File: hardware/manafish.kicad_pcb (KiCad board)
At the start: 4 copper layers, 70 x 90 mm, 118 parts, among them IC1 TPD4EUSB30, IC10 WSEN-PADS_2511020213301, IC11 BMI270, IC12 SHT45-AD1F-R2, IC15 TPS22965DSGR, IC2 TPD4EUSB30, IC3 JXF0-1012NL, IC4 RP2354A, IC5 Ag59824-LPB, IC6 LTV-817S, IC7 LTV-817S, IC8 LTC4162-LAD, IC9 TPSM53604RDA, J1 Conn_01x04_Pin, J11 Conn_01x22_Female, J12 Magnet, J13 Conn_02x06_Odd_Even, J2 SM03B-SRSS-TB, J3 AM32_1, J4 AM32_2, J5 Conn_01x22_Female, J6 Battery, J7 Conn_02x07_Odd_Even, J8 USB_C_Receptacle_USB2.0_14P, J9 Conn_02x08_Odd_Even, Q1 FDMC8327L, Q2 FDMC8327L, Y1 ABM8-272-T3

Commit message: Add switchable ESC power, vertical camera connectors and 3.3 V decoupling
- ESC power switch on the root sheet:
  - Battery input J6 changes to XT60PW-M. New XT60PW-F J14 carries switched
    power to both ESCs.
  - Q3 (onsemi NTMFS5C404NLT1G, 40 V, 0.67 mOhm) is driven by the photovoltaic
    driver IC16 (Vishay VOM1271T) from RP2354A GPIO14 (ESC_PWR_EN) via R31.
  - Soft start C46/D6/R32 keeps Q3 in its SOA while the ESC capacitors charge.
    D7 clamps the gate when the battery is unplugged or the thrusters windmill.
  - Static switch with no current limit: the battery BMS protects. Firmware
    timing rules are in the schematic note and the README.
- Camera connectors J5/J11 are now Molex 501951-2230 (vertical, flip lock).
  The footprint numbers pads n = Molex circuit 23-n so a standard Pi 22-pin
  cable lands GND on pin 1, as on the CM5 IO Board.
- Decoupling: 10 uF + 100 nF at the CM5 3.3 V output, 10 uF at each camera
  supply pin.
- Polyfuses F1-F3 removed; the battery feeds the charger path directly.
- New libraries VOM1271T, NTMFS5C404NL, Molex and Vishay, with 3D models.
- PCB updated from the schematic. The layout will be redone.

Co-Authored-By: Claude Opus 5.5 <noreply@anthropic.com>
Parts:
- removed F1, F2, F3: MF-LSMF260/33X-2, Fuse:Fuse_2920_7451Metric
- added C42: 10uF, Capacitor_SMD:C_0603_1608Metric, F.Cu at (91.6, 108.4)
- added C43: 100n, Capacitor_SMD:C_0402_1005Metric, F.Cu at (91.0, 110.6)
- added C44: 10uF, Capacitor_SMD:C_0603_1608Metric, F.Cu at (91.6, 101.4)
- added C45: 10uF, Capacitor_SMD:C_0603_1608Metric, F.Cu at (91.6, 103.9)
- added C46: 1uF 50V, Capacitor_SMD:C_0603_1608Metric, F.Cu at (81.5, 114.4)
- added D6: 1N4148WS, Diode_SMD:D_SOD-323, F.Cu at (81.7, 108.7)
- added D7: 1N4148WS, Diode_SMD:D_SOD-323, F.Cu at (81.7, 111.6)
- added IC16: VOM1271T, Vishay:Vishay_SOP-4_P2.54mm_VOM1271T, F.Cu at (66.7, 122.4)
- added J14: ESC power, Connector_AMASS:AMASS_XT60PW-F_1x02_P7.20mm_Horizontal, F.Cu at (74.4, 116.5)
- added Q3: NTMFS5C404NL, Package_SO:ONSemi_SO-8FL_488AA, F.Cu at (83.6, 103.7)
- added R31: 180R, Resistor_SMD:R_0402_1005Metric, F.Cu at (81.0, 116.6)
- added R32: 2.2MR, Resistor_SMD:R_0402_1005Metric, F.Cu at (81.0, 118.6)
- J11, J5: footprint CM5IO:Hirose_FH12-22S-0.5SH_1x22-1MP_P0.50mm_Horizontal -> Molex:Molex_501951-2230_1x22-1MP_P0.50mm_Vertical_RPi-CSI
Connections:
- C30 pad 1: /Power Management/BAT+ -> /BAT_IN
- C40 pad 1: /Power Management/BAT+ -> /BAT_IN
- IC4 pad 18: unconnected-(IC4-GPIO14-Pad18) -> /ESC_PWR_EN
- IC8 pad 19: /Power Management/BAT+ -> /BAT_IN
- IC8 pad 20: /Power Management/BAT+ -> /BAT_IN
- J8 pad A4: /VBUS -> unconnected-(J8-VBUS-PadA4)_3
- J8 pad A9: /VBUS -> unconnected-(J8-VBUS-PadA4)_1
- J8 pad B4: /VBUS -> unconnected-(J8-VBUS-PadA4)_2
- J8 pad B9: /VBUS -> unconnected-(J8-VBUS-PadA4)
- R20 pad 2: /Power Management/BAT+ -> /BAT_IN
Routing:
- net /Power Management/BAT+: track 10.4 -> 0.00 mm, vias 6 -> 0
- net /BAT_IN: track 0.00 -> 10.4 mm, vias 0 -> 6
- net /VBUS: track 5.37 -> 0.00 mm
- net (no net): track 0.00 -> 5.37 mm
- added copper zone on F.Cu, net /BAT_IN
- removed copper zone on B.Cu, net /Power Management/BAT+
- removed copper zone on F.Cu, net /Power Management/BAT+

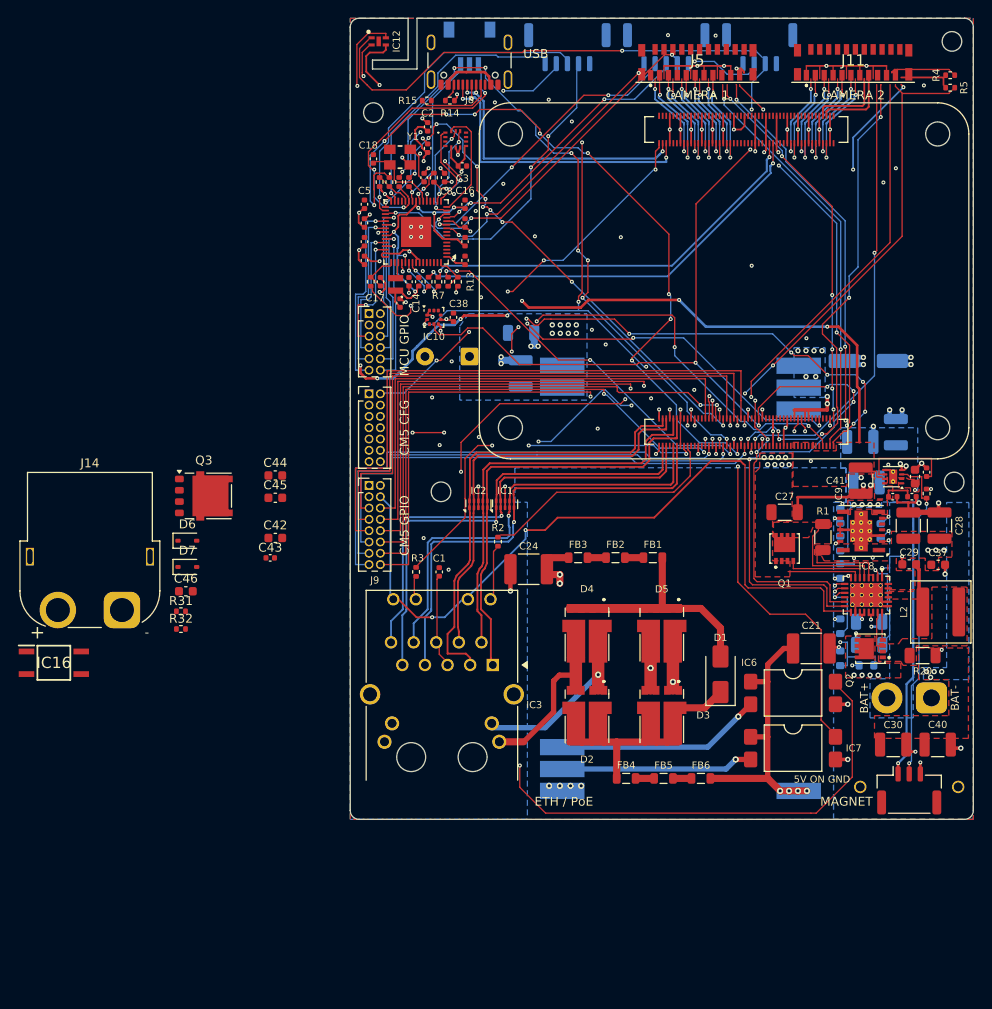
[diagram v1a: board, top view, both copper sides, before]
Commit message: Redo the PCB layout (rev 3): 70 x 109.2 mm, connectors on one side, 45° routing
- All connectors on the top: cameras, USB-C and the magnet switch along the
  top edge, the rest at the bottom around the RJ45, which moves towards the
  centre line; C20 near the centre for the tube radius
- Every part except the PoE module IC5 on the top (reflow one side)
- 45-degree routing only, chamfers at least 1.5 x width, traces bundled to
  keep the planes whole
- Small SHT45 tongue with its bypass cap beside it; planes cut out under L2
  with nothing under it; copper 3.4 mm from the CM5 mounting holes
- Charger and RP2354A regulator laid out per their datasheets
- J3/J4 vertical JST GH (BM05B-GHS-TBT); J8 VBUS label restored
- Edge clearance 0.3 mm, netclass patterns follow the current net names,
  hand-soldered THT GND pins get one thermal spoke
- User.Comments fab/assembly notes and README PCB section updated for rev 3

Co-Authored-By: Claude Opus 5.5 <noreply@anthropic.com>
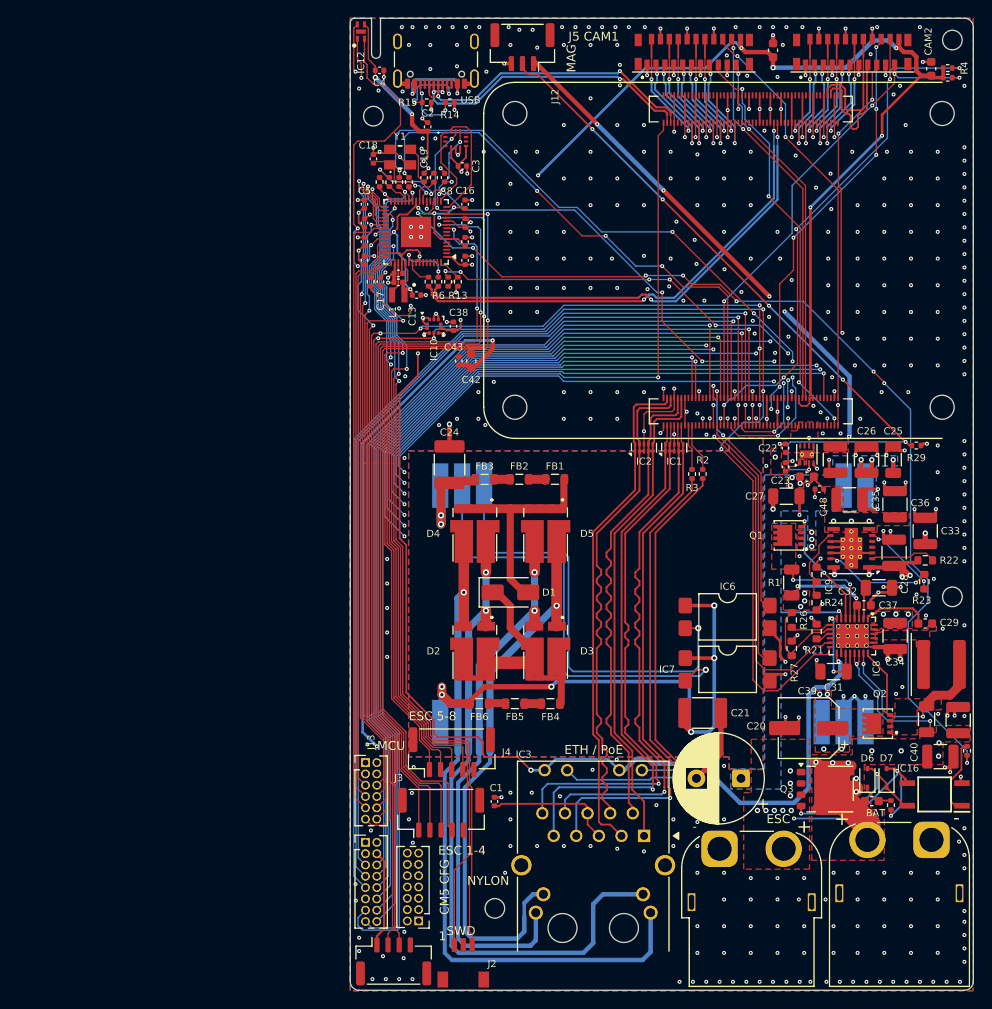
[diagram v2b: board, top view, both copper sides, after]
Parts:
- C20, C25, C26, C31, C32, C34, C35, C36, C39, J1, J2, R21, R22, R23, R24, R25, R26, R27: moved to F.Cu
- J3, J4: footprint Connector_JST:JST_GH_SM05B-GHS-TB_1x05-1MP_P1.25mm_Horizontal -> Connector_JST:JST_GH_BM05B-GHS-TBT_1x05-1MP_P1.25mm_Vertical; moved to F.Cu
- J6: footprint Connector_AMASS:AMASS_XT30PW-M_1x02_P2.50mm_Horizontal -> Connector_AMASS:AMASS_XT60PW-M_1x02_P7.20mm_Horizontal; moved to F.Cu
- moved J1 110.6 mm to (104.9, 156.0)
- moved J2 108.1 mm to (112.7, 158.7)
- moved IC16 100.0 mm to (165.7, 137.2), turned to 180 degrees
- moved J12 94.1 mm to (119.3, 53.2), turned to 180 degrees
- moved R31 89.7 mm to (169.3, 132.3), turned to 90 degrees
- moved J3 89.6 mm to (110.2, 139.2)
- moved C45 88.1 mm to (165.3, 55.7), turned to 90 degrees
- moved R32 82.2 mm to (160.8, 138.4), turned to 90 degrees
- moved D7 82.0 mm to (160.2, 135.3), turned to 90 degrees
- moved D6 80.9 mm to (158.1, 135.3), turned to 90 degrees
- moved C46 80.6 mm to (158.6, 137.9), turned to 180 degrees
- moved J4 80.3 mm to (111.4, 132.4)
- moved Q3 77.2 mm to (153.4, 136.6)
- moved C44 73.5 mm to (147.5, 53.6), turned to 90 degrees
- moved J14 72.3 mm to (141.5, 143.3), turned to 180 degrees
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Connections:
- J8 pad A4: unconnected-(J8-VBUS-PadA4)_3 -> /VBUS
- J8 pad A9: unconnected-(J8-VBUS-PadA4)_1 -> /VBUS
- J8 pad B4: unconnected-(J8-VBUS-PadA4)_2 -> /VBUS
- J8 pad B9: unconnected-(J8-VBUS-PadA4) -> /VBUS
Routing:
- net /RP2354A/+3.3V: track 194.1 -> 364.8 mm, vias 25 -> 28
- net /ESC_PWR_EN: track 0.00 -> 112.9 mm, vias 0 -> 8
- net /Power Management/POE_TYP2_DET: track 127.2 -> 28.2 mm, vias 4 -> 2
- net Net-(IC4-SWCLK): track 16.8 -> 97.0 mm, vias 1 -> 2
- net /Rasperry Pi Compute Module 5/USBOTG: track 43.8 -> 116.8 mm, vias 5 -> 2
- net Net-(IC4-SWDIO): track 29.9 -> 96.4 mm, vias 3 -> 2
- net /Power Management/I2C1_SCL: track 152.4 -> 218.0 mm, vias 9 -> 7
- net /Rasperry Pi Compute Module 5/GPIO7: track 55.0 -> 118.9 mm, vias 1 -> 2
- net /RP2354A/GPIO23: track 21.4 -> 83.9 mm, vias 1 -> 2
- net /Rasperry Pi Compute Module 5/GPIO18: track 55.1 -> 115.2 mm, vias 1 -> 3
- net Net-(IC4-GPIO8): track 30.8 -> 90.0 mm, vias 3 -> 2
- net /RP2354A/GPIO22: track 16.4 -> 74.6 mm, vias 1 -> 2
- net /Ethernet/VC1: track 19.5 -> 77.0 mm, vias 0 -> 1
- net Net-(IC4-GPIO7): track 31.5 -> 87.4 mm, vias 3 -> 2
- net /RP2354A/GPIO28: track 16.7 -> 72.5 mm, vias 1 -> 2
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- added copper zone on In2.Cu, net /BAT_IN
- added copper zone on F.Cu, net /ESC_PWR
- added copper zone on In2.Cu, net /ESC_PWR
- added copper zone on In2.Cu, net /Power Management/+5V_AON
- removed copper zone on B.Cu, net /BAT_IN
- removed copper zone on B.Cu, net /Power Management/+5V_AON
- removed copper zone on In2.Cu, net /Power Management/24V
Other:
- board size 70 x 90 mm -> 70 x 109.2 mm
- board text added: "+"
- board text added: "-"
- board text added: "1"
- board text added: "BAT"
- board text added: "CAM2"
- board text added: "ESC"
- board text added: "ESC 1-4"
- board text added: "ESC 5-8"
- board text added: "FABRICATION JLCPCB 4 layers, 1.6 mm, stackup JLC04161H-7628, 1 oz outer / 0.5 oz inner, ENIG. Board 70 x 109.2 mm. Vias tented on both sides. The exposed-pad vias of IC4, IC8, IC9 and IC15 are open on the top only, through their pads; IC4's 4 sit in the gaps of its paste grid. Everything is tented on the bottom (IC8/IC9 sit above the PoE module IC5). Impedance control +-10 %: L1/L4 100 ohm differ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"
- board text added: "J1 MS5837"
- board text added: "J11 CAMERA 2"
- board text added: "J12 MAGNET"
- board text added: "J14 ESC POWER"
- board text added: "J5 CAM1"
- board text added: "J5 CAMERA 1"
- board text added: "J6 BATTERY"
- board text added: "J8 USB-C"
- board text added: "MAG"
- board text added: "MCU"
- board text added: "NYLON"
- board text added: "rev 3 - 2026-10"
- board text removed: "5V ON GND"
- board text removed: "BAT+"
- board text removed: "BAT-"
- board text removed: "BATTERY"
- board text removed: "CAMERA 1"
- board text removed: "CAMERA 2"
- board text removed: "CM5 GPIO"
- board text removed: "ESC 1"
- board text removed: "ESC 2"
- board text removed: "ETHERNET / PoE"
- board text removed: "FABRICATION JLCPCB 4 layers, 1.6 mm, stackup JLC04161H-7628, 1 oz outer / 0.5 oz inner, ENIG. Board 70 x 90 mm. Vias tented. Exposed-pad vias (IC4, IC8, IC9, IC15) are open on the top through their pads; IC4's 4 sit in the gaps of its paste grid. On the bottom only IC9's are open. Vias in the bottom pads of IC5 (VIN+/VIN-) and C31 (hand-soldered). Impedance control +-10 %: L1/L4 100 ohm different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"
- board text removed: "MAGNET"
- board text removed: "MS5837"
- board text removed: "rev 2 - 2026-10"
